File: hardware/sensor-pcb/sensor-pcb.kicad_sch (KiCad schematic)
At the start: 75 parts, among them J1 Conn_ARM_SWD_TagConnect_TC2030, J2 S5B-PH-SM4-TB, J4 S4B-PH-SM4-TB, M1 PHR-5, M2 SPH-002T-P0.5L, M3 SPH-002T-P0.5L, M4 SPH-002T-P0.5L, M5 SPH-002T-P0.5L, M6 SPH-002T-P0.5L, Q1 BSS138BKSH, SW1 SKRKAHE020, SW2 SKRKAHE020, U1 STM32L476RCTx, U2 AP7354-33W5-7, U4 AP7354-33W5-7

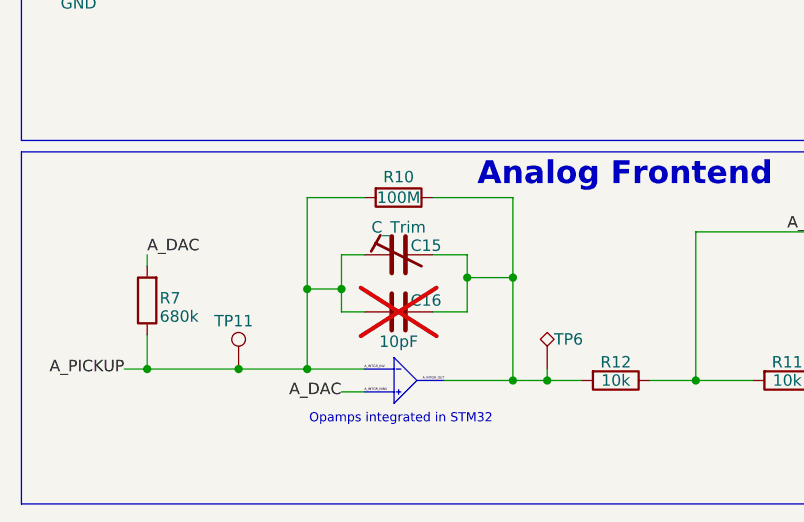
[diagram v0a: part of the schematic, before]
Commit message: Deleted JR200 trimmer library with annoying license. Replaced with custom library. Updated licensing info.
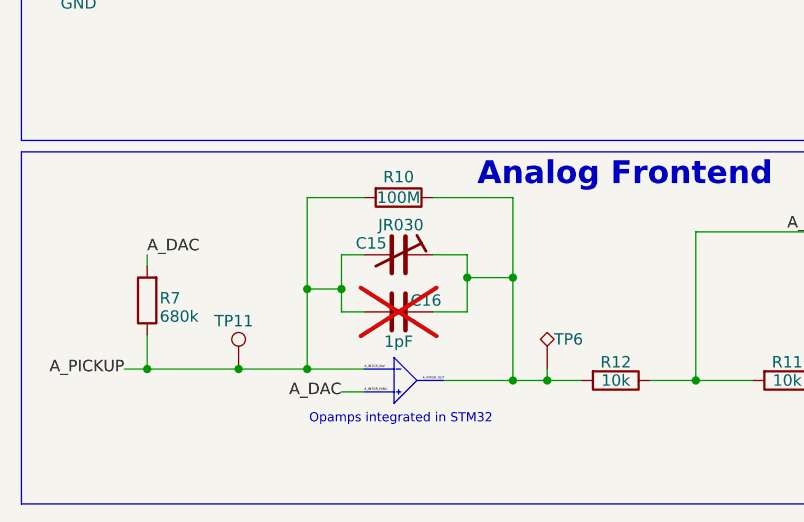
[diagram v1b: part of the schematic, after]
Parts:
- removed C15: C_Trim, JR200:CAPV_JR200, symbol Device:C_Trim
- added C15: JR030, JRx-trimmer:JRx-trimmer, symbol JRx-trimmer:JRx-trimmer
- C16: value 10pF -> 1pF
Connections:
- net A_INTGR_INV: now also C15.2
- net A_INTGR_OUT: now also C15.1
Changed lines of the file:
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@@
 			)
 		)
-		(property "Value" "10pF"
+		(property "Value" "1pF"
 			(at 55.88 184.912 90)
 			(effects
@@
 	)
 	(symbol
+		(lib_id "JRx-trimmer:JRx-trimmer")
+		(at 55.88 175.26 270)
+		(mirror x)
+		(unit 1)
+		(exclude_from_sim no)
+		(in_bom yes)
+		(on_board yes)
+		(dnp no)
+		(property "Reference" "C15"
+			(at 52.832 173.99 90)
+			(effects
+				(font
+					(size 1.27 1.27)
+				)
+			)
+		)
+		(property "Value" "JR030"
+			(at 56.134 171.958 90)
+			(effects
+				(font
+					(size 1.27 1.27)
+				)
+			)
+		)
+		(property "Footprint" "JRx-trimmer:JRx-trimmer"
+			(at 55.88 175.26 0)
+			(effects
+				(font
+					(size 1.27 1.27)
+				)
+				(hide yes)
+			)
+		)
+		(property "Datasheet" "https://www.knowlescapacitors.com/getattachment/727ef5bd-b9cf-4698-a84c-cd891d1f5273/JR-Series"
+			(at 55.88 175.26 0)
+			(effects
+				(font
+					(size 1.27 1.27)
+				)
+				(hide yes)
+			)
+		)
+		(property "Description" "Trimmable capacitor"
+			(at 55.88 175.26 0)
+			(effects
+				(font
+					(size 1.27 1.27)
+				)
+				(hide yes)
+			)
+		)
+		(pin "2"
+		)
+		(pin "1"
+		)
+		(instances
+			(project ""
+				(path "/e73e33d5-48b8-48dd-a5f2-44a1c8331df5"
+					(reference "C15")
+					(unit 1)
+				)
+			)
+		)
+	)
+	(symbol
 		(lib_id "Connector:TestPoint")
 		(at 128.27 27.94 0)
@@
 					(unit 1)
 				)
-			)
-		)
-	)
-	(symbol
-		(lib_id "Device:C_Trim")
-		(at 55.88 175.26 90)
-		(unit 1)
-		(exclude_from_sim no)
-		(in_bom yes)
-		(on_board yes)
-		(dnp no)
-		(property "Reference" "C15"
-			(at 58.928 174.244 90)
-			(effects
-				(font
-					(size 1.27 1.27)
-				)
-			)
-		)
-		(property "Value" "C_Trim"
-			(at 55.88 172.212 90)
-			(effects
-				(font
-					(size 1.27 1.27)
-				)
-			)
-		)
-		(property "Footprint" "JR200:CAPV_JR200"
-			(at 55.88 175.26 0)
-			(effects
-				(font
-					(size 1.27 1.27)
-				)
-				(hide yes)
-			)
-		)
-		(property "Datasheet" "~"
-			(at 55.88 175.26 0)
-			(effects
-				(font
-					(size 1.27 1.27)
-				)
-				(hide yes)
-			)
-		)
-		(property "Description" "Trimmable capacitor"
-			(at 55.88 175.26 0)
-			(effects
-				(font
-					(size 1.27 1.27)
-				)
-				(hide yes)
-			)
-		)
-		(pin "1"
-		)
-		(pin "2"
-		)
-		(instances
-			(project "sensor-pcb"
-				(path "/e73e33d5-48b8-48dd-a5f2-44a1c8331df5"
-					(reference "C15")
-					(unit 1)
-				)

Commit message: Reworked sensor-PCB schematic/layout output jobs
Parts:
- C1, C11, C13, C14, C19, C2, C20, C3, C4: MFPN (none) -> GCM188R71E105KA64D
- C10, C5, C6, C7, C8, C9: MFPN (none) -> GCM155R71C104KA55D
- C12: MFPN (none) -> GCM21BR71C475KA73L
- C15: MFPN (none) -> JR030
- C16: MFPN (none) -> GCM1555C1H1R0CA16J
- C17: MFPN (none) -> GCM1885G1H112FA16D
- C18: MFPN (none) -> GCM1885C1H222FA16D
- D1: MFPN (none) -> APT3216LZGCK
- D2: value APTD3216LSURCK -> APT3216LSECK/J3-PRV; MFPN (none) -> APT3216LSECK/J3-PRV
- J2: MFPN (none) -> S5B-PH-SM4-TB
- J4: MFPN (none) -> S4B-PH-SM4-TB; now not fitted
- M1: MFPN (none) -> PHR-5
- M2, M3, M4, M5, M6: value SPH-002T-P0.5L -> ASPHSPH24K102; MFPN (none) -> ASPHSPH24K102
- Q1: MFPN (none) -> BSS138BKSH; now not fitted
- R1, R8: MFPN (none) -> CRCW0603510RFKEA
- R10: MFPN (none) -> CRCW0603100MJPEAHR
- R11, R12, R15: MFPN (none) -> CRCW060310K0FKEA
- R13, R14, R3, R5: MFPN (none) -> CRCW060310K0FKEA; now not fitted
- R16, R2, R9: MFPN (none) -> CRCW06030000Z0EA
- R4, R6: MFPN (none) -> CRCW06035K10FKEA
- R7: MFPN (none) -> CRCW0603680KFKEA
- SW1, SW2: MFPN (none) -> SKRKAHE020
- TP10, TP12, TP14, TP17, TP6, TP8: value TestPoint_Alt -> TP_Keystone_5015; MFPN (none) -> 5015
- U1: MFPN (none) -> STM32L476RCT6
- U2, U4: MFPN (none) -> AP7354-33W5-7

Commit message: Implemented kicad CI/CD. Removed committed exports except schematic PDF.
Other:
- moved on the sheet: TP13
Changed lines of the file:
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@@
 	(wire
 		(pts
+			(xy 113.03 91.44) (xy 113.03 92.71)
+		)
+		(stroke
+			(width 0)
+			(type default)
+		)
+	)
+	(wire
+		(pts
 			(xy 107.95 34.29) (xy 107.95 29.21)
 		)
@@
 	(wire
 		(pts
-			(xy 116.84 92.71) (xy 116.84 91.44)
+			(xy 123.19 92.71) (xy 123.19 91.44)
 		)
 		(stroke
@@
 		)
 	)
+	(wire
+		(pts
+			(xy 111.76 92.71) (xy 113.03 92.71)
+		)
+		(stroke
+			(width 0)
+			(type default)
+		)
+	)
 	(polyline
 		(pts
@@
 	(symbol
 		(lib_id "Connector:TestPoint")
-		(at 116.84 91.44 0)
+		(at 123.19 91.44 0)
 		(unit 1)
 		(exclude_from_sim no)
@@
 		(dnp no)
 		(property "Reference" "TP13"
-			(at 118.4663 86.106 0)
+			(at 124.8163 86.106 0)
 			(effects
 				(font
@@
 		)
 		(property "Value" "TestPoint"
-			(at 114.3 86.8681 0)
+			(at 120.65 86.8681 0)
 			(effects
 				(font
@@
 		)
 		(property "Footprint" "TestPoint:TestPoint_Pad_D1.0mm"
-			(at 121.92 91.44 0)
+			(at 128.27 91.44 0)
 			(effects
 				(font
@@
 		)
 		(property "Datasheet" "~"
-			(at 121.92 91.44 0)
+			(at 128.27 91.44 0)
 			(effects
 				(font
@@
 		)
 		(property "Description" "test point"
-			(at 116.84 91.44 0)
+			(at 123.19 91.44 0)
 			(effects
 				(font
@@
 		)
 		(property "MFPN" ""
-			(at 116.84 91.44 0)
+			(at 123.19 91.44 0)
 			(effects
 				(font
@@
 	(symbol
 		(lib_id "power:GND")
-		(at 116.84 92.71 0)
+		(at 123.19 92.71 0)
 		(unit 1)
 		(exclude_from_sim no)
@@
 		(dnp no)
 		(property "Reference" "#PWR055"
-			(at 116.84 99.06 0)
+			(at 123.19 99.06 0)
 			(effects
 				(font
@@
 		)
 		(property "Value" "GND"
-			(at 116.84 96.266 0)
+			(at 123.19 96.266 0)
 			(effects
 				(font
@@
 		)
 		(property "Footprint" ""
-			(at 116.84 92.71 0)
+			(at 123.19 92.71 0)
 			(effects
 				(font
@@
 		)
 		(property "Datasheet" ""
-			(at 116.84 92.71 0)
+			(at 123.19 92.71 0)
 			(effects
 				(font
@@
 		)
 		(property "Description" "Power symbol creates a global label with name \"GND\" , ground"
-			(at 116.84 92.71 0)
+			(at 123.19 92.71 0)
 			(effects
 				(font
@@
 	)
 	(symbol
+		(lib_id "power:PWR_FLAG")
+		(at 111.76 92.71 90)
+		(unit 1)
+		(exclude_from_sim no)
+		(in_bom yes)
+		(on_board yes)
+		(dnp no)
+		(fields_autoplaced yes)
+		(property "Reference" "#FLG05"
+			(at 109.855 92.71 0)
+			(effects
+				(font
+					(size 1.27 1.27)
+				)
+				(hide yes)
+			)
+		)
+		(property "Value" "PWR_FLAG"
+			(at 107.95 92.7099 90)
+			(effects
+				(font
+					(size 1.27 1.27)
+				)
+				(justify left)
+			)
+		)
+		(property "Footprint" ""
+			(at 111.76 92.71 0)
+			(effects
+				(font
+					(size 1.27 1.27)
+				)
+				(hide yes)
+			)
+		)
+		(property "Datasheet" "~"
+			(at 111.76 92.71 0)
+			(effects
+				(font
+					(size 1.27 1.27)
+				)
+				(hide yes)
+			)
+		)
+		(property "Description" "Special symbol for telling ERC where power comes from"
+			(at 111.76 92.71 0)
+			(effects
+				(font
+					(size 1.27 1.27)
+				)
+				(hide yes)
+			)
+		)
+		(pin "1"
+		)
+		(instances
+			(project "sensor-pcb"
+				(path "/e73e33d5-48b8-48dd-a5f2-44a1c8331df5"
+					(reference "#FLG05")
+					(unit 1)
+				)
+			)
+		)
+	)
+	(symbol
 		(lib_id "power:+3V3")
 		(at 229.87 26.67 0)
@@
 					(unit 1)
 				)
+			)
+		)
+	)
+	(symbol
+		(lib_id "power:VBUS")
+		(at 113.03 91.44 0)
+		(unit 1)
+		(exclude_from_sim no)
+		(in_bom yes)
+		(on_board yes)
+		(dnp no)
+		(fields_autoplaced yes)
+		(property "Reference" "#PWR062"
+			(at 113.03 95.25 0)
+			(effects
+				(font
+					(size 1.27 1.27)
+				)
+				(hide yes)
+			)
+		)
+		(property "Value" "VBUSA"
+			(at 113.03 86.36 0)
+			(effects
+				(font
+					(size 1.27 1.27)
+				)
+			)
+		)
+		(property "Footprint" ""
+			(at 113.03 91.44 0)
+			(effects
+				(font
+					(size 1.27 1.27)
+				)
+				(hide yes)
+			)
+		)
+		(property "Datasheet" ""
+			(at 113.03 91.44 0)
+			(effects
+				(font
+					(size 1.27 1.27)
+				)
+				(hide yes)
+			)
+		)
+		(property "Description" "Power symbol creates a global label with name \"VBUS\""
+			(at 113.03 91.44 0)
+			(effects
+				(font
+					(size 1.27 1.27)
+				)
+				(hide yes)
+			)
+		)
+		(pin "1"
+		)
+		(instances
+			(project "sensor-pcb"
+				(path "/e73e33d5-48b8-48dd-a5f2-44a1c8331df5"
+					(reference "#PWR062")
+					(unit 1)
+				)

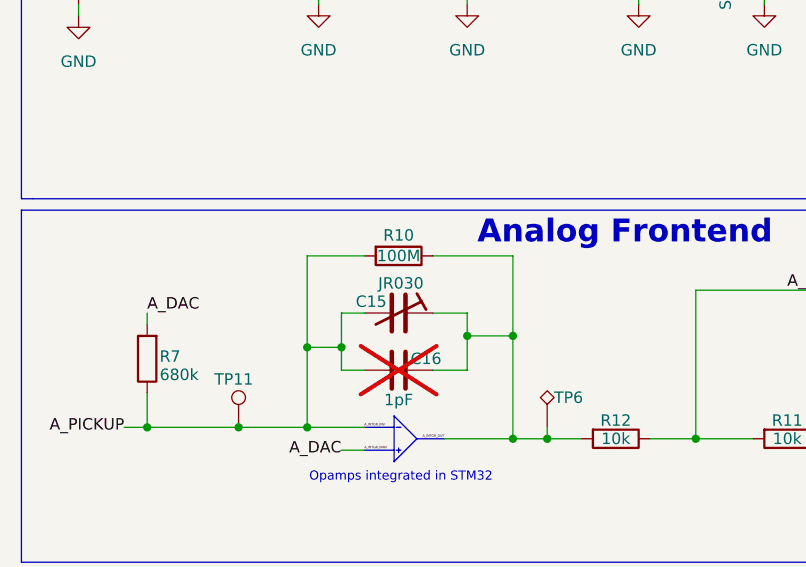
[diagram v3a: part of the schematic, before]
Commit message: Changed trimmer back to JR200
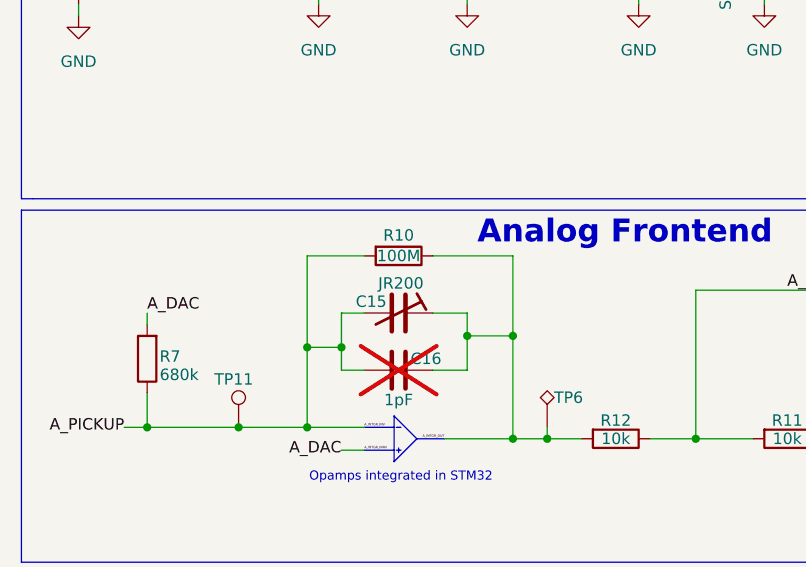
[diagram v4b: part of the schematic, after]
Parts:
- C15: value JR030 -> JR200; MFPN JR030 -> JR200
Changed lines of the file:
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@@
 			)
 		)
-		(property "Value" "JR030"
+		(property "Value" "JR200"
 			(at 56.134 171.958 90)
 			(effects
@@
 			)
 		)
-		(property "MFPN" "JR030"
+		(property "MFPN" "JR200"
 			(at 55.88 175.26 90)
 			(effects
